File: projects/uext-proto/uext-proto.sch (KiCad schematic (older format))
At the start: 8 parts, among them CON1 UEXT-5V, CON2 UEXT-BREADBOARD, CON3 UEXT-5V, J1 CONN_01X11, U1 LM1117-3.3

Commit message: added latest projects
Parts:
- removed C2: C, Capacitors_THT:C_Axial_L5.1mm_D3.1mm_P7.50mm_Horizontal, symbol C
- removed C?: CP, Capacitors_THT:CP_Axial_L10.0mm_D6.0mm_P15.00mm_Horizontal, symbol CP
- removed CON2: UEXT-BREADBOARD, limero-lib:UEXT-BREADBOARD, symbol UEXT-BREADBOARD
- removed CON3: UEXT-5V, limero-lib:UEXT, symbol UEXT-5V
- added C2: CP, Capacitors_THT:CP_Radial_D8.0mm_P5.00mm, symbol CP
- added C3: C, Capacitors_THT:C_Disc_D8.0mm_W5.0mm_P5.00mm, symbol C
- C1: footprint Capacitors_THT:CP_Axial_L10.0mm_D6.0mm_P15.00mm_Horizontal -> Capacitors_THT:CP_Radial_D8.0mm_P5.00mm
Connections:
- wire segments 45 -> 35
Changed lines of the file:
@@
 EESchema Schematic File Version 2
+LIBS:limero
 LIBS:power
 LIBS:device
@@
 LIBS:contrib
 LIBS:valves
-LIBS:nodemcu
-LIBS:uext
-LIBS:limero
-LIBS:uext-breadboard-cache
+LIBS:uext-proto-cache
 EELAYER 25 0
 EELAYER END
@@
 $EndDescr
 $Comp
-L UEXT-BREADBOARD CON2
-U 1 1 59711C4F
-P 5800 2550
-F 0 "CON2" H 5400 2250 40  0000 C CNN
-F 1 "UEXT-BREADBOARD" H 5950 2250 40  0000 C CNN
-F 2 "limero-lib:UEXT-BREADBOARD" H 5500 2550 60  0001 C CNN
-F 3 "" H 5500 2550 60  0000 C CNN
-	1    5800 2550
-	1    0    0    -1
-$EndComp
-$Comp
 L LM1117-3.3 U1
-U 1 1 59711F8A
+U 1 1 5971D2CC
 P 3500 2700
 F 0 "U1" H 3600 2450 50  0000 C CNN
@@
 $EndComp
 $Comp
-L CP C1
-U 1 1 59712108
+L CP C2
+U 1 1 5971D2CD
 P 4000 2900
-F 0 "C1" H 4025 3000 50  0000 L CNN
+F 0 "C2" H 4025 3000 50  0000 L CNN
 F 1 "CP" H 4025 2800 50  0000 L CNN
-F 2 "Capacitors_THT:CP_Axial_L10.0mm_D6.0mm_P15.00mm_Horizontal" H 4038 2750 50  0001 C CNN
+F 2 "Capacitors_THT:CP_Radial_D8.0mm_P5.00mm" H 4038 2750 50  0001 C CNN
 F 3 "" H 4000 2900 50  0001 C CNN
 	1    4000 2900
@@
 $EndComp
 $Comp
-L C C2
-U 1 1 597121A1
+L C C3
+U 1 1 5971D2CE
 P 4350 2900
-F 0 "C2" H 4375 3000 50  0000 L CNN
+F 0 "C3" H 4375 3000 50  0000 L CNN
 F 1 "C" H 4375 2800 50  0000 L CNN
-F 2 "Capacitors_THT:C_Axial_L5.1mm_D3.1mm_P7.50mm_Horizontal" H 4388 2750 50  0001 C CNN
+F 2 "Capacitors_THT:C_Disc_D8.0mm_W5.0mm_P5.00mm" H 4388 2750 50  0001 C CNN
 F 3 "" H 4350 2900 50  0001 C CNN
 	1    4350 2900
@@
 $Comp
 L GND #PWR01
-U 1 1 597121E0
+U 1 1 5971D2CF
 P 3750 3200
 F 0 "#PWR01" H 3750 2950 50  0001 C CNN
@@
 $Comp
 L +5V #PWR02
-U 1 1 59712200
-P 3000 2700
-F 0 "#PWR02" H 3000 2550 50  0001 C CNN
-F 1 "+5V" H 3000 2840 50  0000 C CNN
-F 2 "" H 3000 2700 50  0001 C CNN
-F 3 "" H 3000 2700 50  0001 C CNN
-	1    3000 2700
-	1    0    0    -1
-$EndComp
-Wire Wire Line
-	6250 2750 6600 2750
-Wire Wire Line
-	6250 2650 6600 2650
-Wire Wire Line
-	6250 2550 6600 2550
-Wire Wire Line
-	6250 2450 6600 2450
-Wire Wire Line
-	6250 2350 6600 2350
-Wire Wire Line
-	5450 2350 5100 2350
-Wire Wire Line
-	5450 2450 5100 2450
-Wire Wire Line
-	5450 2550 5100 2550
-Wire Wire Line
-	5100 2650 5450 2650
-Wire Wire Line
-	5450 2750 5100 2750
-Wire Wire Line
-	3000 2700 3200 2700
+U 1 1 5971D2D0
+P 2700 2700
+F 0 "#PWR02" H 2700 2550 50  0001 C CNN
+F 1 "+5V" H 2700 2840 50  0000 C CNN
+F 2 "" H 2700 2700 50  0001 C CNN
+F 3 "" H 2700 2700 50  0001 C CNN
+	1    2700 2700
+	1    0    0    -1
+$EndComp
+Wire Wire Line
+	2700 2700 3200 2700
 Wire Wire Line
 	3500 3000 3500 3200
 Wire Wire Line
-	3000 3200 4350 3200
+	2700 3200 4350 3200
 Wire Wire Line
 	4000 3200 4000 3050
@@
 $Comp
 L +3V3 #PWR03
-U 1 1 59712659
+U 1 1 5971D2D1
 P 4550 2700
 F 0 "#PWR03" H 4550 2550 50  0001 C CNN
@@
 Connection ~ 4350 2700
 $Comp
-L UEXT-5V CON3
-U 1 1 59712B3F
-P 5850 2550
-F 0 "CON3" H 5700 2850 40  0000 C CNN
-F 1 "UEXT-5V" H 6000 2250 40  0000 C CNN
-F 2 "limero-lib:UEXT" H 5550 2550 60  0001 C CNN
-F 3 "" H 5550 2550 60  0000 C CNN
-	1    5850 2550
-	1    0    0    -1
-$EndComp
-$Comp
 L UEXT-5V CON1
-U 1 1 59712BEF
+U 1 1 5971D2D2
 P 3550 3950
 F 0 "CON1" H 3400 4250 40  0000 C CNN
@@
 $Comp
 L +5V #PWR04
-U 1 1 59712CF4
+U 1 1 5971D2D3
 P 3050 3750
 F 0 "#PWR04" H 3050 3600 50  0001 C CNN
@@
 $Comp
 L GND #PWR05
-U 1 1 59712D2F
+U 1 1 5971D2D4
 P 4400 3700
 F 0 "#PWR05" H 4400 3450 50  0001 C CNN
@@
 $Comp
 L +5V #PWR06
-U 1 1 5971B2A4
+U 1 1 5971D2D5
 P 5450 3700
 F 0 "#PWR06" H 5450 3550 50  0001 C CNN
@@
 $Comp
 L GND #PWR07
-U 1 1 5971B2C4
+U 1 1 5971D2D6
 P 5250 3750
 F 0 "#PWR07" H 5250 3500 50  0001 C CNN
@@
 $Comp
 L CONN_01X11 J1
-U 1 1 5971B947
+U 1 1 5971D2D7
 P 6100 4150
 F 0 "J1" H 6100 4750 50  0000 C CNN
@@
 $Comp
 L +3V3 #PWR08
-U 1 1 5971C070
+U 1 1 5971D2D8
 P 5650 3650
 F 0 "#PWR08" H 5650 3500 50  0001 C CNN
@@
 	5650 3650 5900 3650
 $Comp
-L CP C?
-U 1 1 5971C216
-P 3000 2850
-F 0 "C?" H 3025 2950 50  0000 L CNN
-F 1 "CP" H 3025 2750 50  0000 L CNN
-F 2 "Capacitors_THT:CP_Axial_L10.0mm_D6.0mm_P15.00mm_Horizontal" H 3038 2700 50  0001 C CNN
-F 3 "" H 3000 2850 50  0001 C CNN
-	1    3000 2850
-	1    0    0    -1
-$EndComp
-Wire Wire Line
-	3000 3000 3000 3200
+L CP C1
+U 1 1 5971D2D9
+P 2700 2850
+F 0 "C1" H 2725 2950 50  0000 L CNN
+F 1 "CP" H 2725 2750 50  0000 L CNN
+F 2 "Capacitors_THT:CP_Radial_D8.0mm_P5.00mm" H 2738 2700 50  0001 C CNN
+F 3 "" H 2700 2850 50  0001 C CNN
+	1    2700 2850
+	1    0    0    -1
+$EndComp
 Connection ~ 3500 3200
+Wire Wire Line
+	2700 3000 2700 3200
 $EndSCHEMATC

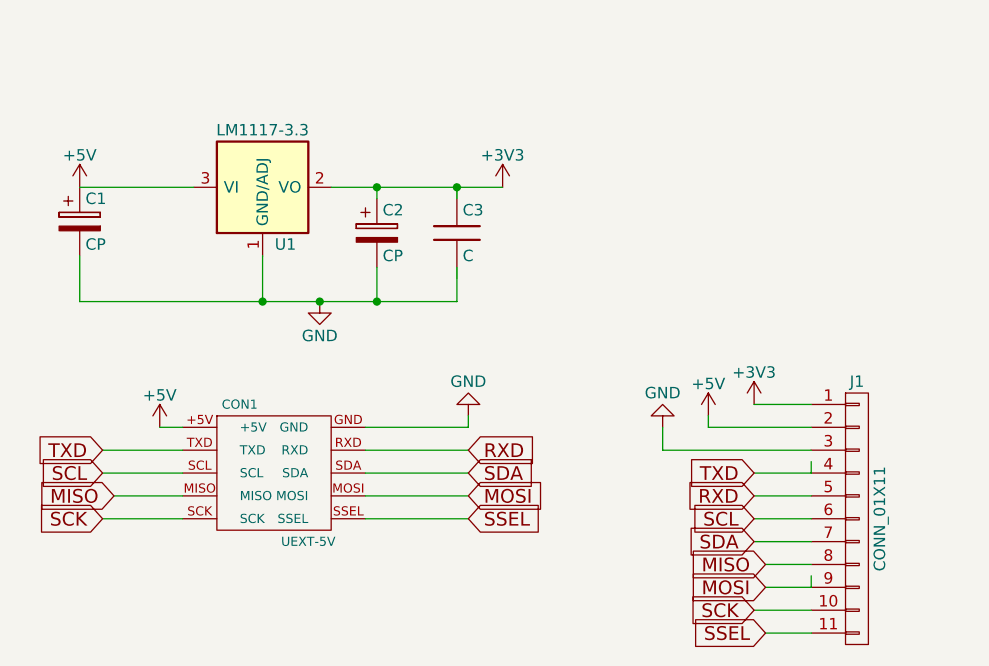
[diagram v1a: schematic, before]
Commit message: made proto board for UEXT connector
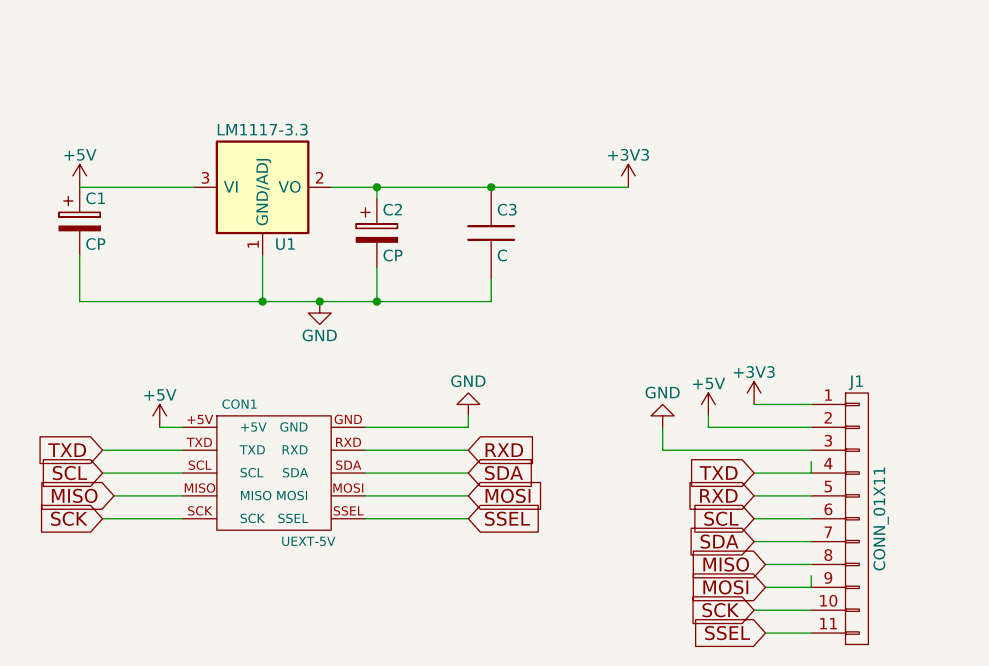
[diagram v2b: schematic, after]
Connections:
- wire segments 35 -> 34
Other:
- moved on the sheet: C3
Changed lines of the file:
@@
 L C C3
 U 1 1 5971D2CE
-P 4350 2900
-F 0 "C3" H 4375 3000 50  0000 L CNN
-F 1 "C" H 4375 2800 50  0000 L CNN
-F 2 "Capacitors_THT:C_Disc_D8.0mm_W5.0mm_P5.00mm" H 4388 2750 50  0001 C CNN
-F 3 "" H 4350 2900 50  0001 C CNN
-	1    4350 2900
+P 4500 2900
+F 0 "C3" H 4525 3000 50  0000 L CNN
+F 1 "C" H 4525 2800 50  0000 L CNN
+F 2 "Capacitors_THT:C_Disc_D8.0mm_W5.0mm_P5.00mm" H 4538 2750 50  0001 C CNN
+F 3 "" H 4500 2900 50  0001 C CNN
+	1    4500 2900
 	1    0    0    -1
 $EndComp
@@
 	3500 3000 3500 3200
 Wire Wire Line
-	2700 3200 4350 3200
+	2700 3200 4500 3200
 Wire Wire Line
 	4000 3200 4000 3050
 Connection ~ 3750 3200
-Wire Wire Line
-	4350 3200 4350 3050
 Connection ~ 4000 3200
 Wire Wire Line
-	3800 2700 4550 2700
+	3800 2700 5100 2700
 Wire Wire Line
 	4000 2700 4000 2750
-Wire Wire Line
-	4350 2700 4350 2750
 Connection ~ 4000 2700
 $Comp
 L +3V3 #PWR03
 U 1 1 5971D2D1
-P 4550 2700
-F 0 "#PWR03" H 4550 2550 50  0001 C CNN
-F 1 "+3V3" H 4550 2840 50  0000 C CNN
-F 2 "" H 4550 2700 50  0001 C CNN
-F 3 "" H 4550 2700 50  0001 C CNN
-	1    4550 2700
-	1    0    0    -1
-$EndComp
-Connection ~ 4350 2700
+P 5100 2700
+F 0 "#PWR03" H 5100 2550 50  0001 C CNN
+F 1 "+3V3" H 5100 2840 50  0000 C CNN
+F 2 "" H 5100 2700 50  0001 C CNN
+F 3 "" H 5100 2700 50  0001 C CNN
+	1    5100 2700
+	1    0    0    -1
+$EndComp
+Connection ~ 4500 2700
 $Comp
 L UEXT-5V CON1
@@
 Wire Wire Line
 	2700 3000 2700 3200
+Wire Wire Line
+	4500 3200 4500 3100
 $EndSCHEMATC
